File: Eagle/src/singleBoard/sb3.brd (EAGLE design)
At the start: 83.5 x 114.3 mm, 54 parts, among them J1 UJ2-BH-1-TH, Q2 IRFD9120, U1 GY-521MPU6050

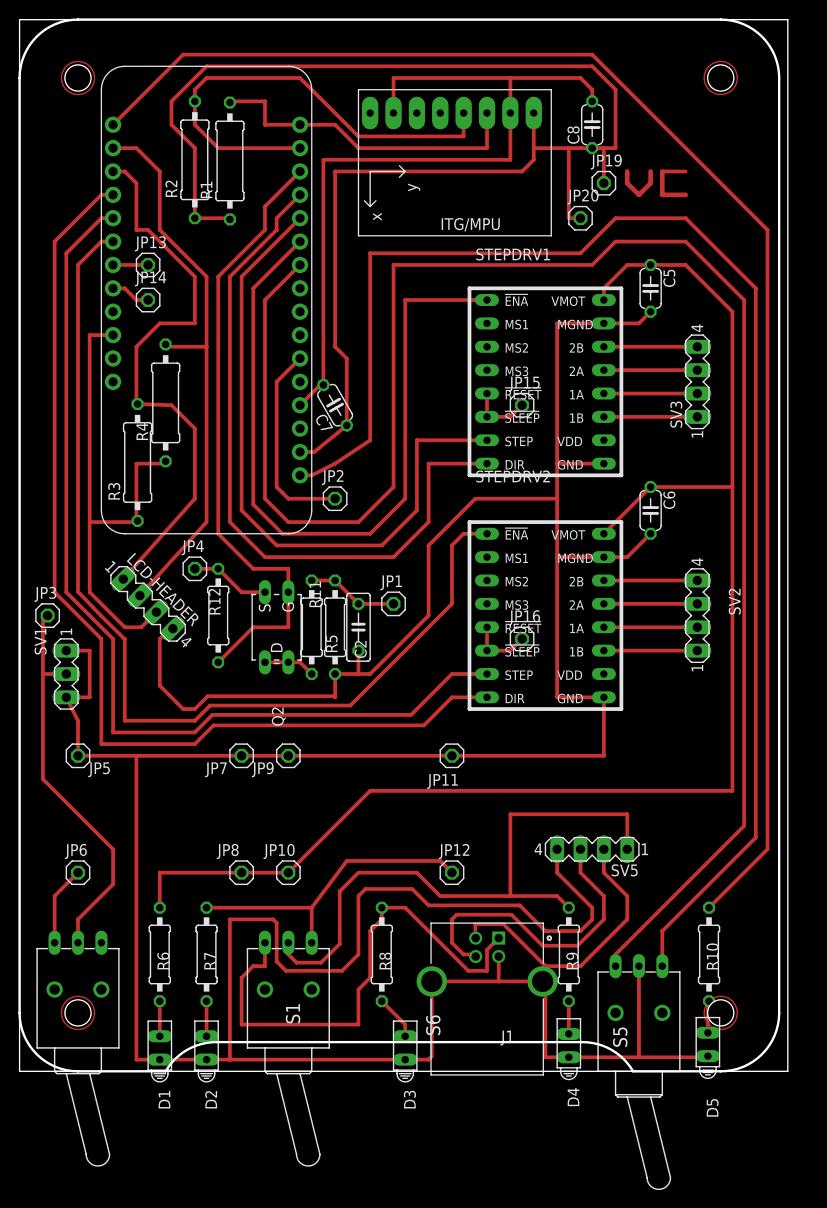
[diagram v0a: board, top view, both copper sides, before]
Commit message: updated single board, new switches
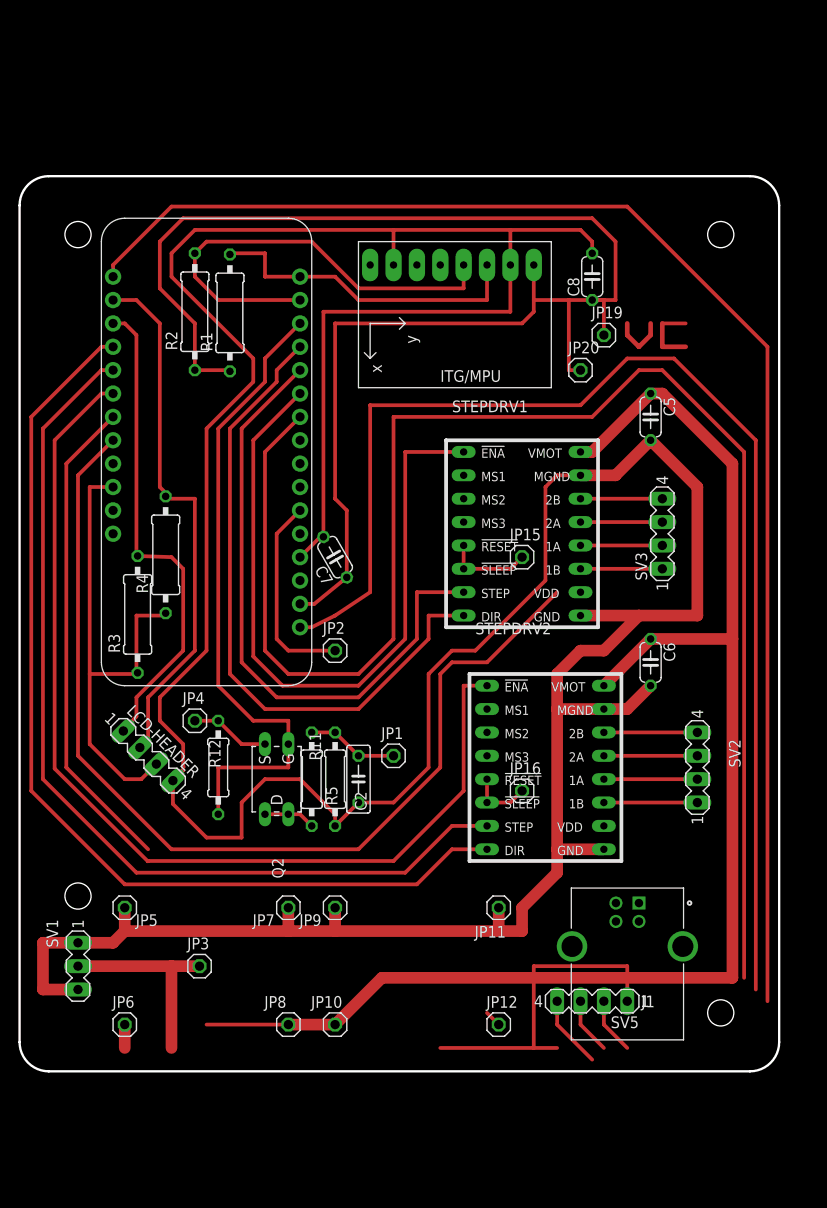
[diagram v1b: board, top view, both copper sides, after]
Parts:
- removed D1, D2, D3, D4, D5: HLMP6, display-hp:HLMP6
- removed JP13, JP14: (no value), pinhead:1X01
- removed R10, R6, R7, R8, R9: (no value), rcl:0207/10
- removed S1, S5, S6: (no value), switch:9070-1W
- moved JP3 41.5 mm to (19.6, 11.4)
- moved SV1 31.8 mm to (6.35, 11.4)
- moved JP10 17.3 mm to (34.3, 5.08)
- moved JP11 17.3 mm to (52.1, 17.8)
- moved JP12 17.3 mm to (52.1, 5.08)
- moved JP5 17.3 mm to (11.4, 17.8)
- moved JP6 17.3 mm to (11.4, 5.08)
- moved JP7 17.3 mm to (29.2, 17.8)
- moved JP8 17.3 mm to (29.2, 5.08)
- moved JP9 17.3 mm to (34.3, 17.8)
- moved SV3 16.9 mm to (69.8, 58.4)
- moved STEPDRV1 16.7 mm to (55.9, 59.7)
- moved C8 16.5 mm to (62.2, 86.4)
- moved MS2 16.5 mm to (31.8, 41.9)
- moved R1 16.5 mm to (22.9, 82.4)
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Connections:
- removed net N$2: C7.2, C8.2, MS2.4, U1.ADO, U1.GND
- removed net N$52: D4.K, R9.1
- removed net N$53: D1.K, R6.1
- removed net N$54: D2.K, R7.1
- removed net N$55: D3.K, R8.1
- removed net N$57: D5.K, R10.1
- new net N$38: JP6.1
- new net N$39: SV5.4
- net N$28: no longer R10.2
- net N$31: no longer S5.3
- net N$32: no longer S6.2
- net N$36: no longer JP13.1
- net N$37: no longer JP14.1
- net N$4: no longer S5.1
- net N$40: now also J1.4, J1.SH1, J1.SH2; no longer JP6.1, S6.3
- net N$41: no longer R6.2
- net N$45: no longer R7.2, S1.1
- net N$48: no longer R9.2, S1.2
- net N$56: no longer R8.2, S1.3
- net N$9: now also C7.2, C8.2, MS2.4, U1.ADO, U1.GND; no longer D1.A, D2.A, D3.A, D4.A, D5.A, J1.4, J1.SH1, J1.SH2, S5.2, SV5.4
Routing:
- net N$37: track 4.34 -> 109.7 mm
- net N$2: track 84.5 -> 0.00 mm
- net N$56: track 55.5 -> 0.00 mm
- net N$36: track 3.81 -> 52.8 mm
- net N$45: track 33.5 -> 1.80 mm
- net N$48: track 66.5 -> 35.6 mm
- net N$23: track 33.7 -> 6.45 mm
- net N$22: track 30.7 -> 6.19 mm
- net N$32: track 43.0 -> 22.1 mm
- net N$31: track 187.7 -> 168.7 mm
- net N$4: track 153.5 -> 136.4 mm
- net N$11: track 61.9 -> 52.9 mm
- net N$40: track 8.67 -> 0.44 mm
- net N$39: track 0.00 -> 7.93 mm
- net N$9: track 424.8 -> 432.2 mm
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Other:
- board size 83.5 x 114.3 mm -> 82.5 x 97.3 mm

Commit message: finalization of single board design, plus remoted switches and usb jack
finalization of single board design, plus remoted switches and usb jack
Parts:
- removed J1: UJ2-BH-1-TH, UJ2-BH-1-TH:CUI_UJ2-BH-1-TH
- removed Q2: IRFD9120, transistor-small-signal:C370-01
- removed SV1: (no value), con-lstb:MA03-1
- removed SV5: (no value), con-lstb:MA04-1
- added 12V-1, 12V-2, 12V-3, 12V-4, GND, JP13, JP14, JP17, JP18: (no value), pinhead:1X01
- added BAT-PWR: (no value), con-lstb:MA03-1
- added CON1: (no value), con-harting:CON16
- added D1, D3: 1N5400, diode:DO201-15
- added ESP-USB: (no value), con-lstb:MA04-1
- added FET: IRFD9120, transistor-small-signal:C370-01
- added R6: (no value), rcl:0207/10
- moved R3 18.3 mm to (15.1, 67.8), turned to 75 degrees
- moved JP3 14.0 mm to (33.5, 10.2)
- moved JP2 13.1 mm to (38.7, 58.0)
- moved JP1 13.0 mm to (27.9, 36.8)
- moved R12 12.0 mm to (17.8, 44.5), turned to 285 degrees
- moved C7 11.7 mm to (36.8, 67.3), turned to 105 degrees
- moved JP20 11.7 mm to (68.6, 85.1)
- moved JP4 11.4 mm to (19.1, 49.5)
- moved R4 8.98 mm to (17.1, 65.0), turned to 75 degrees
- moved SV2 6.84 mm to (67.3, 35.6)
- moved C6 6.35 mm to (73.7, 48.3)
- moved STEPDRV2 5.24 mm to (53.3, 35.6)
- moved JP15 3.81 mm to (50.8, 55.9)
- moved JP16 3.81 mm to (50.8, 30.5)
- moved R5 2.84 mm to (30.5, 34.3), turned to 235 degrees
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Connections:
- removed net N$39: SV5.4
- removed net N$48: SV5.1
- removed net N$56: J1.1
- removed net VDD: STEPDRV1.10, STEPDRV2.10
- new net N$1: MS2.24, STEPDRV1.10
- new net N$2: CON1.5, R6.2
- new net N$26: BAT-PWR.2, D1.A
- new net N$42: 12V-1.1, 12V-3.1, JP10.1, JP8.1, R6.1
- new net N$43: CON1.7, JP12.1
- new net N$44: 12V-2.1, C6.1, STEPDRV2.16
- new net N$46: BAT-PWR.1, BAT-PWR.3, D3.C
- new net N$55: CON1.9, ESP-USB.1
- net 3V: now also CON1.2
- net N$22: now also CON1.11, ESP-USB.2; no longer J1.2, SV5.2
- net N$23: now also CON1.13, ESP-USB.3; no longer J1.3, SV5.3
- net N$24: now also FET.S; no longer Q2.S
- net N$27: now also JP17.1, JP6.1; no longer MS2.20, STEPDRV2.8
- net N$28: now also CON1.4
- net N$29: now also STEPDRV2.8; no longer STEPDRV2.7
- net N$31: now also CON1.3
- net N$32: now also D1.C, JP13.1; no longer SV1.2
- net N$34: now also STEPDRV2.7; no longer STEPDRV2.1
- net N$36: now also MS2.20, STEPDRV2.10; no longer MS2.23
- net N$37: now also MS2.23, STEPDRV2.1; no longer MS2.24
- net N$38: now also CON1.15, JP18.1; no longer JP6.1
- net N$4: now also CON1.1
- net N$40: now also CON1.10, CON1.8; no longer J1.4, J1.SH1, J1.SH2
- net N$41: now also C2.1, C5.2, C6.2, C7.2, C8.2, CON1.12, CON1.14, D3.A, ESP-USB.4, GND.1, JP11.1, JP5.1, JP7.1, JP9.1, LCD-HEADER.4, MS2.4, R11.1, STEPDRV1.15, STEPDRV1.9, STEPDRV2.15, STEPDRV2.9, U1.ADO, U1.GND; no longer C5.1, C6.1, JP10.1, JP8.1, STEPDRV1.16, STEPDRV2.16
- net N$45: now also 12V-4.1, C5.1, STEPDRV1.16; no longer JP12.1
- net N$51: now also FET.D, FET.D1; no longer Q2.D, Q2.D1
- net N$6: now also FET.G; no longer Q2.G
- net N$9: now also CON1.16, JP14.1; no longer C2.1, C5.2, C6.2, C7.2, C8.2, JP11.1, JP5.1, JP7.1, JP9.1, LCD-HEADER.4, MS2.4, R11.1, STEPDRV1.15, STEPDRV1.9, STEPDRV2.15, STEPDRV2.9, SV1.1, SV1.3, U1.ADO, U1.GND
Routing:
- net N$9: track 432.2 -> 4.34 mm
- net N$41: track 153.5 -> 501.1 mm
- net N$27: track 108.0 -> 6.35 mm
- net N$1: track 6.13 -> 106.7 mm
- net N$36: track 52.8 -> 114.0 mm
- net 3V: track 161.8 -> 207.2 mm
- net N$43: track 0.00 -> 35.8 mm
- net N$48: track 35.6 -> 0.00 mm
- net N$42: track 0.00 -> 29.3 mm
- net N$28: track 152.5 -> 126.3 mm
- net N$4: track 136.4 -> 112.1 mm
- net N$31: track 168.7 -> 147.3 mm
- net N$55: track 0.00 -> 21.0 mm
- net N$2: track 0.00 -> 20.3 mm
- net N$34: track 109.9 -> 90.0 mm
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
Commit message: upload from Doug's PC
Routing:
- net N$4: track 112.1 -> 113.5 mm
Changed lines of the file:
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@@
 </layers>
 <board>
-<fusionsync huburn="a.cGVyc29uYWw6dWUyZDlmNmRl" projecturn="a.cGVyc29uYWw6dWUyZDlkNTAxIzIwMTgxMDI0MTU2NDI4OTAx" f3durn="urn:adsk.wipprod:dm.lineage:RVMtdEYxSvOPFW49h7ULsg" pcbguid="49d98df1-49b2-45fb-9c3f-6a5aa2b8ca4d" lastpulledtime="2019-02-27T19:32:19Z" lastsyncedchangeguid="2b95e2a0-3dcb-4e46-8abe-5d507ab46a9a"/>
+<fusionsync huburn="a.cGVyc29uYWw6dWUyZDlmNmRl" projecturn="a.cGVyc29uYWw6dWUyZDlkNTAxIzIwMTgxMDI0MTU2NDI4OTAx" f3durn="urn:adsk.wipprod:dm.lineage:RVMtdEYxSvOPFW49h7ULsg" pcbguid="49d98df1-49b2-45fb-9c3f-6a5aa2b8ca4d" lastpulledtime="2019-03-17T19:19:13Z" lastsyncedchangeguid="24049744-be62-3583-beae-4fb7246fa9cf"/>
 <plain>
 <dimension x1="0" y1="118.11" x2="82.55" y2="118.11" x3="41.275" y3="120.65" textsize="1.778" layer="1" unit="inch"/>
 <dimension x1="-7.62" y1="0" x2="-7.62" y2="96.52" x3="-8.89" y3="48.26" textsize="1.778" layer="1" unit="inch"/>
-<hole x="77.47" y="92.202" drill="2.8448"/>
-<hole x="5.08" y="20.32" drill="2.8448"/>
-<hole x="5.08" y="92.202" drill="2.8448"/>
-<hole x="77.47" y="5.08" drill="2.8448"/>
+<hole x="77.47" y="92.202" drill="2.845"/>
+<hole x="5.08" y="20.32" drill="2.845"/>
+<hole x="5.08" y="92.202" drill="2.845"/>
+<hole x="77.47" y="5.08" drill="2.845"/>
 <wire x1="82.55" y1="94.107" x2="79.375" y2="97.282" width="0.254" layer="20" curve="90"/>
 <wire x1="79.375" y1="97.282" x2="3.175" y2="97.282" width="0.254" layer="20"/>
@@
 </element>
 <element name="R11" library="rcl" library_urn="urn:adsk.eagle:library:334" package="0207/10" package3d_urn="urn:adsk.eagle:package:23491/1" value="" x="33.02" y="34.29" smashed="yes" rot="R55">
-<attribute name="NAME" x="32.93711875" y="36.828646875" size="1.27" layer="25" ratio="10" rot="R55"/>
+<attribute name="NAME" x="32.93711875" y="33.018646875" size="1.27" layer="25" ratio="10" rot="R55"/>
 <attribute name="SPICEPREFIX" value="R" x="106.876459375" y="-63.9363625" size="1.778" layer="27" rot="R55" display="off"/>
 <attribute name="VALUE" x="106.09999375" y="-66.15235625" size="1.27" layer="27" ratio="10" rot="R55"/>
@@
 <wire x1="30.48" y1="50.8" x2="31.75" y2="50.8" width="0.4064" layer="1"/>
 <wire x1="31.75" y1="50.8" x2="34.29" y2="55.88" width="0.4064" layer="1"/>
-<wire x1="34.29" y1="60.49931875" x2="34.29" y2="55.88" width="0.4064" layer="1"/>
+<wire x1="34.29" y1="55.88" x2="34.29" y2="60.49931875" width="0.4064" layer="1"/>
 <wire x1="37.4874" y1="64.856546875" x2="34.29" y2="60.49931875" width="0.4064" layer="1"/>
 <wire x1="17.78" y1="82.55" x2="17.643903125" y2="78.11904375" width="0.4064" layer="1"/>
@@
 <contactref element="CON1" pad="1"/>
 <wire x1="74.93" y1="38.1" x2="74.93" y2="36.83" width="0.4064" layer="1"/>
+<wire x1="30.48" y1="48.26" x2="30.48" y2="49.6824" width="0.1524" layer="1"/>
 </signal>
 <signal name="N$3">

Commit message: final fixesbefore release to manufacturing
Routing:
- net N$4: track 113.5 -> 112.1 mm

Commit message: trivial change to force update
this file has length 171,438
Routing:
- net N$39: track 501.1 -> 504.6 mm
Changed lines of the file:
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@@
 <?xml version="1.0" encoding="utf-8"?>
 <!DOCTYPE eagle SYSTEM "eagle.dtd">
-<eagle version="9.3.0">
+<eagle version="9.4.0">
 <drawing>
 <settings>
@@
 <wire x1="60.96" y1="49.53" x2="62.23" y2="50.8" width="1.27" layer="1"/>
 <wire x1="54.61" y1="45.72" x2="58.42" y2="49.53" width="1.27" layer="1"/>
-<wire x1="25.4" y1="8.89" x2="24.13" y2="7.62" width="0.4064" layer="1"/>
-<wire x1="24.13" y1="7.62" x2="24.13" y2="2.54" width="0.4064" layer="1"/>
+<wire x1="24.13" y1="8.89" x2="24.13" y2="2.54" width="0.4064" layer="1"/>
 <wire x1="57.15" y1="2.54" x2="24.13" y2="2.54" width="0.4064" layer="1"/>
 <wire x1="59.69" y1="5.08" x2="57.15" y2="2.54" width="0.4064" layer="1"/>
@@
 <wire x1="80.01" y1="13.97" x2="80.01" y2="20.32" width="0.4064" layer="1"/>
 <wire x1="67.31" y1="5.08" x2="73.66" y2="11.43" width="0.4064" layer="1"/>
-<wire x1="25.4" y1="8.89" x2="22.86" y2="11.43" width="1.27" layer="1"/>
-<wire x1="22.86" y1="17.78" x2="22.86" y2="11.43" width="1.27" layer="1"/>
+<wire x1="20.32" y1="17.78" x2="20.32" y2="8.89" width="1.27" layer="1"/>
 <wire x1="16.51" y1="33.02" x2="27.432" y2="33.02" width="0.4064" layer="1"/>
 <wire x1="16.51" y1="33.02" x2="13.97" y2="30.48" width="0.4064" layer="1"/>
@@
 <wire x1="57.15" y1="64.77" x2="54.61" y2="62.23" width="0.4064" layer="1"/>
 <wire x1="55.88" y1="40.64" x2="54.61" y2="41.91" width="1.27" layer="1"/>
-<wire x1="11.43" y1="17.78" x2="22.86" y2="17.78" width="1.27" layer="1"/>
-<wire x1="22.86" y1="17.78" x2="29.21" y2="17.78" width="1.27" layer="1"/>
+<wire x1="11.43" y1="17.78" x2="20.32" y2="17.78" width="1.27" layer="1"/>
+<wire x1="20.32" y1="17.78" x2="29.21" y2="17.78" width="1.27" layer="1"/>
 <wire x1="29.21" y1="17.78" x2="34.29" y2="17.78" width="1.27" layer="1"/>
 <wire x1="34.29" y1="17.78" x2="52.07" y2="17.78" width="1.27" layer="1"/>
-<wire x1="25.4" y1="8.89" x2="27.94" y2="8.89" width="1.27" layer="1"/>
+<wire x1="20.32" y1="8.89" x2="24.13" y2="8.89" width="1.27" layer="1"/>
+<wire x1="24.13" y1="8.89" x2="27.94" y2="8.89" width="1.27" layer="1"/>
 </signal>
 </signals>
